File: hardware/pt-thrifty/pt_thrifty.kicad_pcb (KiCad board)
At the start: 2 copper layers, 25.4 x 31.6 mm, 23 parts, among them J1 Conn_01x09, J2 Conn_01x09, J3 SJ-43514-SMT-TR, SW1 PTS636 SM50J SMTR LFS, SW2 SW_Push_Shielded, U2 MCP6273T-E/CH

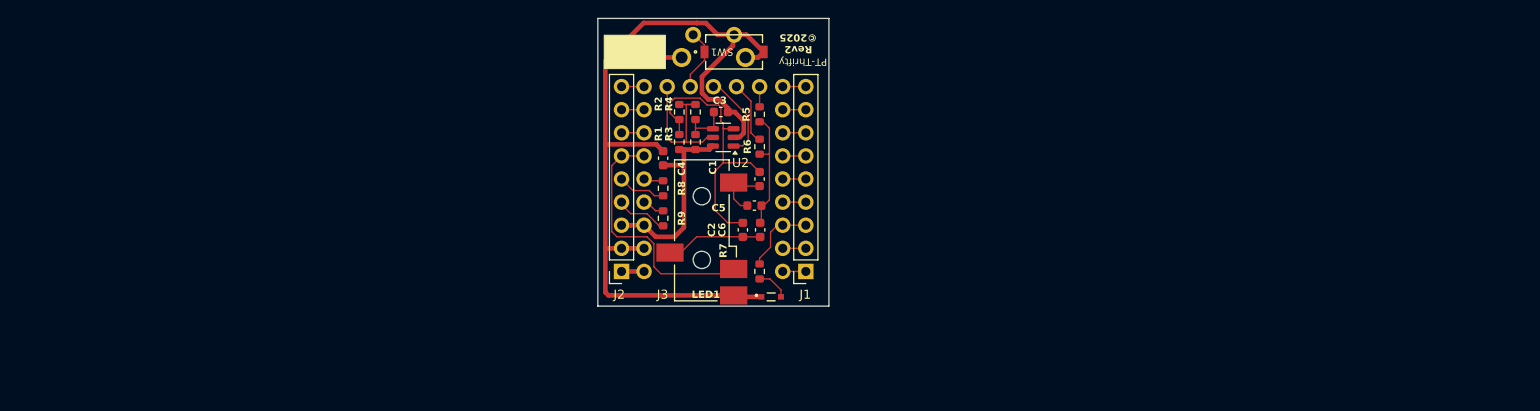
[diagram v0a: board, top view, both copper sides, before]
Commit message: Re-import symbols into PCB layout
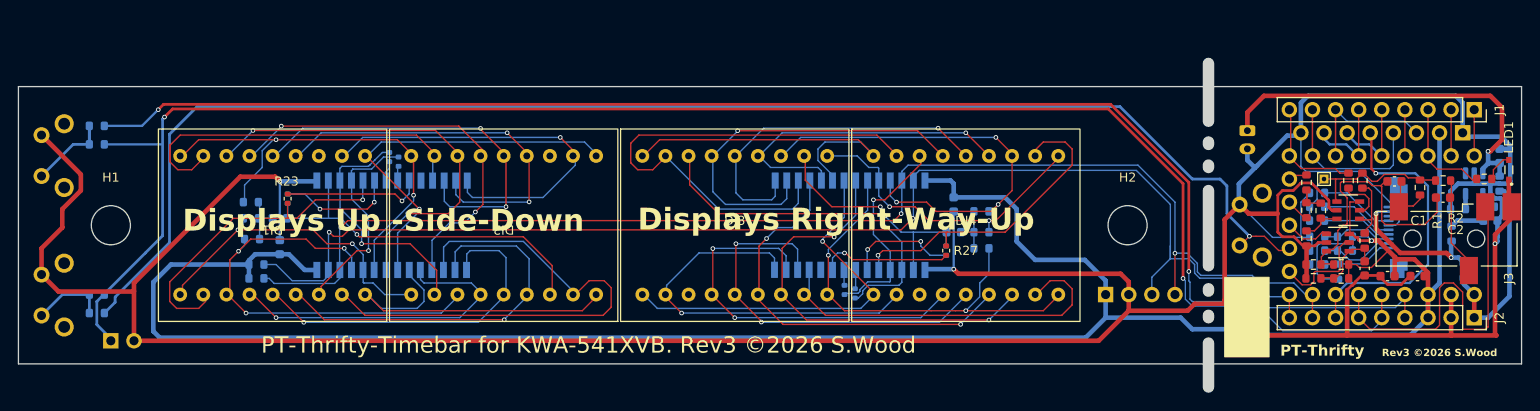
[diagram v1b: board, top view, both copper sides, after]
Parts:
- removed C6: 100nF, Capacitor_SMD:C_0603_1608Metric
- added C7: 10uF, Capacitor_SMD:C_0603_1608Metric, B.Cu at (166.3, 89.2)
- added C8: 10uF, Capacitor_SMD:C_0603_1608Metric, B.Cu at (92.2, 93.9)
- added C81: 1uF, Capacitor_SMD:C_0603_1608Metric, B.Cu at (225.3, 90.9)
- added C82: 1uF, Capacitor_SMD:C_0603_1608Metric, B.Cu at (226.3, 83.8)
- added D1: D, Diode_SMD:D_0603_1608Metric, B.Cu at (166.3, 92.2)
- added D2: D, Diode_SMD:D_0603_1608Metric, B.Cu at (92.2, 90.7)
- added DI1: KWA-541XVB, DeliveryBos LEDs:KWA-541XVB, F.Cu at (91.4, 91.4)
- added DI2: KWA-541XVB, DeliveryBos LEDs:KWA-541XVB, F.Cu at (116.8, 91.4)
- added DI3: KWA-541XVB, DeliveryBos LEDs:KWA-541XVB, F.Cu at (142.2, 91.4)
- added DI4: KWA-541XVB, DeliveryBos LEDs:KWA-541XVB, F.Cu at (167.6, 91.4)
- added H1: MountingHole, MountingHole:MountingHole_4.3mm_M4, F.Cu at (73.7, 91.4)
- added H2: MountingHole, MountingHole:MountingHole_4.3mm_M4, F.Cu at (185.4, 91.4)
- added J4: Conn_01x08, Connector_PinSocket_2.54mm:PinSocket_1x08_P2.54mm_Vertical, B.Cu at (222.2, 81.3)
- added J5: Conn_01x04, Connector_PinSocket_2.54mm:PinSocket_1x04_P2.54mm_Vertical, B.Cu at (183.0, 99.1)
- added J6: Conn_01x02, Connector_PinSocket_2.54mm:PinSocket_1x02_P2.54mm_Vertical, B.Cu at (73.7, 104.1)
- added J81: Conn_01x02, Connector_JST:JST_PH_B2B-PH-K_1x02_P2.00mm_Vertical, B.Cu at (198.6, 81.0)
- added J99: Conn_01x10, Connector_FFC-FPC:Amphenol_F32Q-1A7x1-11010_1x10-1MP_P0.5mm_Horizontal, B.Cu at (217.0, 91.7)
- added R10: 100K, Resistor_SMD:R_0603_1608Metric, F.Cu at (206.7, 89.8)
- added R11: 100K, Resistor_SMD:R_0603_1608Metric, F.Cu at (205.1, 92.9)
- added R12: 100K, Resistor_SMD:R_0603_1608Metric, F.Cu at (211.5, 93.1)
- added R13: 100K, Resistor_SMD:R_0603_1608Metric, F.Cu at (211.2, 86.5)
- added R14: 100R, Resistor_SMD:R_0603_1608Metric, F.Cu at (209.7, 86.5)
- added R15: 0R, Resistor_SMD:R_0603_1608Metric, B.Cu at (72.1, 101.1)
- added R16: 0R, Resistor_SMD:R_0603_1608Metric, B.Cu at (72.1, 99.1)
- added R17: 0R, Resistor_SMD:R_0603_1608Metric, B.Cu at (72.1, 80.5)
- added R18: 0R, Resistor_SMD:R_0603_1608Metric, B.Cu at (72.1, 82.5)
- added R20: 0R, Resistor_SMD:R_0402_1005Metric, B.Cu at (93.1, 88.5)
- added R21: 0R, Resistor_SMD:R_0402_1005Metric, B.Cu at (104.3, 83.9)
- added R22: 0R, Resistor_SMD:R_0402_1005Metric, B.Cu at (105.3, 84.5)
- added R23: 0R, Resistor_SMD:R_0402_1005Metric, F.Cu at (93.1, 88.5)
- added R24: 0R, Resistor_SMD:R_0402_1005Metric, B.Cu at (165.5, 94.2)
- added R25: 0R, Resistor_SMD:R_0402_1005Metric, B.Cu at (155.4, 98.9)
- added R26: 0R, Resistor_SMD:R_0402_1005Metric, B.Cu at (154.3, 98.6)
- added R27: 0R, Resistor_SMD:R_0402_1005Metric, F.Cu at (165.5, 94.2)
- added R28: 10K, Resistor_SMD:R_0603_1608Metric, B.Cu at (89.7, 95.8)
- added R29: 10K, Resistor_SMD:R_0603_1608Metric, B.Cu at (89.7, 97.3)
- added R30: 47K, Resistor_SMD:R_0603_1608Metric, B.Cu at (169.4, 89.9)
- added R31: 47K, Resistor_SMD:R_0603_1608Metric, B.Cu at (169.4, 92.2)
- added R32: 47K, Resistor_SMD:R_0603_1608Metric, B.Cu at (169.4, 94.0)
- added R33: 47K, Resistor_SMD:R_0603_1608Metric, B.Cu at (89.2, 93.0)
- added R34: 47K, Resistor_SMD:R_0603_1608Metric, B.Cu at (89.1, 90.7)
- added R35: 47K, Resistor_SMD:R_0603_1608Metric, B.Cu at (89.1, 88.9)
- added R81: 2.00K-1%, Resistor_SMD:R_0603_1608Metric, B.Cu at (221.7, 89.7)
- added R82: 100R, Resistor_SMD:R_0603_1608Metric, B.Cu at (226.6, 89.4)
- added R83: 100R, Resistor_SMD:R_0603_1608Metric, B.Cu at (221.0, 92.4)
- added R84: 100R, Resistor_SMD:R_0603_1608Metric, B.Cu at (226.3, 86.9)
- added R90: 100R, Resistor_SMD:R_0603_1608Metric, B.Cu at (222.4, 96.4)
- added R91: 100K, Resistor_SMD:R_0603_1608Metric, B.Cu at (208.5, 96.5)
- added R92: 100K, Resistor_SMD:R_0603_1608Metric, B.Cu at (206.3, 95.8)
- added R93: 100K, Resistor_SMD:R_0603_1608Metric, B.Cu at (209.3, 94.2)
- added R94: 100K, Resistor_SMD:R_0603_1608Metric, B.Cu at (206.3, 94.2)
- added R95: 100K, Resistor_SMD:R_0603_1608Metric, B.Cu at (209.3, 92.7)
- added R96: 100K, Resistor_SMD:R_0603_1608Metric, B.Cu at (206.3, 92.7)
- added R97: 100R, Resistor_SMD:R_0603_1608Metric, B.Cu at (206.2, 90.9)
- added R98: 100R, Resistor_SMD:R_0603_1608Metric, B.Cu at (206.2, 89.4)
- added R99: 100R, Resistor_SMD:R_0603_1608Metric, B.Cu at (206.2, 87.9)
- added SW3: SW_Push_Shielded, Button_Switch_THT:SW_Tactile_SPST_Angled_PTS645Vx31-2LFS, B.Cu at (66.0, 81.5)
- added TP1: TestPoint, TestPoint:TestPoint_THTPad_1.0x1.0mm_Drill0.5mm, F.Cu at (207.0, 86.4)
- added U3: MCP6273T-E/CH, MCP6273T_E_CH:SOT-23-6_MC_MCH-L, F.Cu at (209.7, 89.8)
- added U4: HT16K33A-28SOIC, HT16K33A-28SSOP:SOIC28-1.27-11.5X17.5MM, B.Cu at (154.9, 91.4)
- added U5: HT16K33A-28SOIC, HT16K33A-28SSOP:SOIC28-1.27-11.5X17.5MM, B.Cu at (104.5, 91.4)
- added U80: MCP73832-2-OT, Package_TO_SOT_SMD:SOT-23-5, B.Cu at (223.5, 86.9)
- C1, C2, C5: value 100nF -> 1uF
- J3: footprint PicoTimecode_PCB_Rev2:CUI_SJ-43514-SMT-TR -> SJ-43514-SMT-TR:CUI_SJ-43514-SMT-TR
- LED1: footprint footprints:LED_LTST-S220GKT_LTO -> LTST_S220GKT:LED_LTST-S220GKT_LTO
- R1, R2: value 10K -> 100R
- R3, R4: value 10K -> 100K
- R5: value 2.10K-1% -> 2.00K-1%
- R8: value 22R -> 2.00K-1%
- R9: value 22R -> 2.49K-1%
- SW1: value PTS636 SM50J SMTR LFS -> SW_Push_Shielded; footprint PicoTimecode_PCB_Rev2:SW_PTS636_CNK -> Button_Switch_THT:SW_Tactile_SPST_Angled_PTS645Vx31-2LFS; moved to B.Cu
- U2: footprint Package_TO_SOT_SMD:SOT-23-6 -> MCP6273T_E_CH:SOT-23-6_MC_MCH-L
- moved U1 94.2 mm to (225.1, 100.4), turned to 90 degrees
- moved J2 93.9 mm to (223.5, 101.6), turned to -90 degrees
- moved J3 86.1 mm to (227.6, 89.4), turned to 180 degrees
- moved R2 84.3 mm to (220.1, 86.5), turned to 0 degrees
- moved LED1 82.3 mm to (227.3, 85.3), turned to 90 degrees
- moved R1 81.6 mm to (217.6, 87.3), turned to -90 degrees
- moved C4 80.7 mm to (214.0, 97.0), turned to 180 degrees
- moved SW2 80.6 mm to (66.0, 96.9), turned to -90 degrees
- moved R7 80.3 mm to (224.6, 86.4), turned to 0 degrees
- moved C2 77.0 mm to (220.1, 88.4), turned to 180 degrees
- moved J1 75.6 mm to (223.5, 78.7), turned to -90 degrees
- moved C5 73.3 mm to (217.3, 97.0)
- moved C3 72.8 mm to (211.5, 96.2), turned to -90 degrees
- moved R3 72.2 mm to (208.9, 95.8), turned to 180 degrees
- moved R8 70.7 mm to (205.1, 86.7)
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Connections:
- net Net-(J1-Pin_5) renamed /SPI0_DC
- net Net-(J1-Pin_6) renamed /SPI0_CSn
- net Net-(J1-Pin_7) renamed /SPI0_SCK
- net Net-(J1-Pin_8) renamed /SPI0_TX
- net Net-(J1-Pin_9) renamed /AMP_nEN1
- net Net-(J2-Pin_7) renamed /SPI0_RST
- net Net-(J2-Pin_8) renamed /I2C1_SCLK
- net Net-(J2-Pin_9) renamed /I2C1_SDA
- C5 pad 1: /IN_OUT_L -> GND
- C5 pad 2: Net-(C5-Pad2) -> +3.3V
- J2 pad 4: Net-(J2-Pin_4) -> /ROT_SW
- J2 pad 5: Net-(J2-Pin_5) -> /CLAP_SW
- R1 pad 1: +3.3V -> /OUTPUT
- R1 pad 2: /IN -> /IN_OUT_L
- R2 pad 1: /IN -> /OUTPUT
- R2 pad 2: /AMP_CS -> /IN_OUT_R
- R3 pad 2: /VREF -> /IN
- R4 pad 1: /VREF -> /IN
- R4 pad 2: /AMP_CS -> GND
- R5 pad 1: /LTC_TX -> +3.3V
- R5 pad 2: Net-(C5-Pad2) -> /VREF
- R6 pad 1: /nLTC_TX -> /VREF
- R6 pad 2: Net-(C5-Pad2) -> GND
- R8 pad 1: Net-(U1-GPIO28) -> /LTC_TX
- R8 pad 2: Net-(J2-Pin_5) -> Net-(R10-Pad1)
- R9 pad 1: Net-(U1-GPIO29) -> /nLTC_TX
- R9 pad 2: Net-(J2-Pin_4) -> Net-(R10-Pad1)
- SW1 pad 1: /KEYA -> GND
- SW1 pad 2: GND -> /KEYA
- SW2 pad 2: /KEYA -> Net-(R15-Pad2)
- U1 pad 14: Net-(U1-GPIO28) -> /CLAP_SW
- U1 pad 15: Net-(U1-GPIO29) -> /ROT_SW
- U1 pad 23: /AMP_CS -> /AMP_nEN0
- U2 pad 5: /AMP_CS -> /AMP_nEN0
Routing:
- net GND: track 101.3 -> 434.8 mm, vias 0 -> 3
- net +3.3V: track 23.4 -> 265.5 mm, vias 0 -> 1
- net /CLAP_SW: track 0.00 -> 189.8 mm, vias 0 -> 2
- net /ROT_SW: track 0.00 -> 164.4 mm, vias 0 -> 2
- net /KEYA: track 6.86 -> 157.1 mm, vias 0 -> 1
- net /I2C1_SCLK: track 2.48 -> 144.0 mm, vias 0 -> 3
- net /I2C1_SDA: track 2.48 -> 143.0 mm, vias 0 -> 2
- net /time-bar/HM_ROW8: track 0.00 -> 57.4 mm
- net /time-bar/SF_ROW8: track 0.00 -> 57.4 mm
- net /time-bar/HM_ROW2: track 0.00 -> 49.7 mm, vias 0 -> 2
- net /time-bar/HM_ROW0: track 0.00 -> 49.3 mm, vias 0 -> 3
- net /time-bar/SF_ROW2: track 0.00 -> 49.1 mm, vias 0 -> 2
- net /time-bar/SF_ROW0: track 0.00 -> 49.1 mm, vias 0 -> 3
- net /time-bar/SF_ROW3: track 0.00 -> 46.4 mm, vias 0 -> 2
- net /time-bar/HM_ROW3: track 0.00 -> 46.4 mm, vias 0 -> 2
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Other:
- board size 25.4 x 31.6 mm -> 165.2 x 35.6 mm
- board text added: "0"
- board text added: "0.0"
- board text added: "0.3"
- board text added: "0.4"
- board text added: "0.6"
- board text added: "0.65"
- board text added: "0.9"
- board text added: "1.2 inch"
- board text added: "16-Segment {dblquote}Time-Bar{dblquote} - for KWA-541XVB modules"
- board text added: "2026-07-28 © Simon Wood"
- board text added: "4.8"
- board text added: "5.2"
- board text added: "6.5 inch"
- board text added: "Displays Rig ht-Way-Up"
- board text added: "Displays Up -Side-Down"
- board text added: "PT Thrifty - lowest cost TimeCode"
- board text added: "PT-Thrifty-Timebar for KWA-541XVB. Rev3 ©2026 S.Wood"
- board text added: "Rev 3"
- board text added: "Rev3 ©2026 S.Wood"
- board text removed: "Rev2 ©2025"

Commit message: Add 3D models and pin-1 markings
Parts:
- LED1: footprint LTST_S220GKT:LED_LTST-S220GKT_LTO -> LTST_S220GKT:LED_LTST-S220GKT_LTO-L
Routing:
- net +3.3V: track 265.5 -> 266.7 mm
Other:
- board text added: "PT-Thrifty-Timebar for KWA-541AVB. Rev3 ©2026 S.Wood"
- board text removed: "PT-Thrifty-Timebar for KWA-541XVB. Rev3 ©2026 S.Wood"
